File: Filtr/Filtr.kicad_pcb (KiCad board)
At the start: 2 copper layers, 80 x 50 mm, 41 parts, among them J1 Jack-DC, J2 Conn_01x04_Pin, SW3 RotaryEncoder_Switch, U1 TPS562200, U2 STM32G030K6Tx

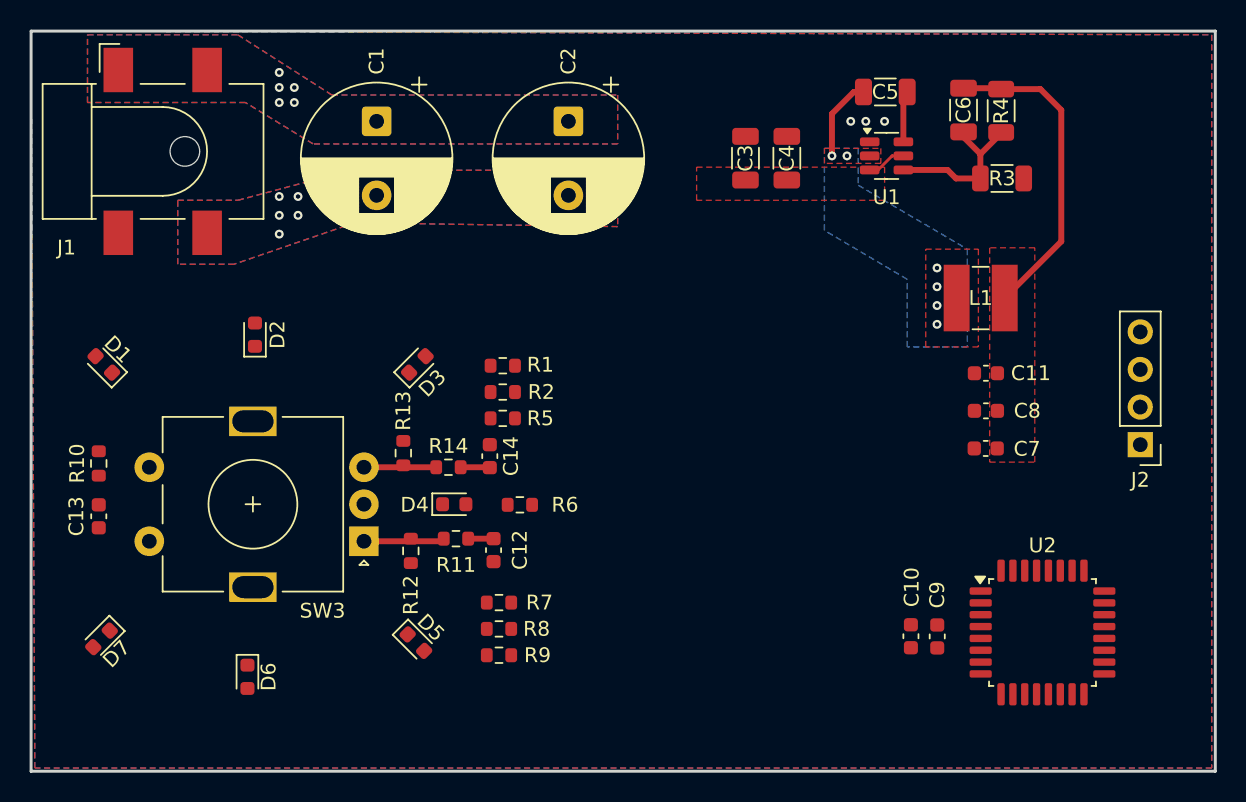
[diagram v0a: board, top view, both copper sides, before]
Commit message: Vymazani CubeIDE
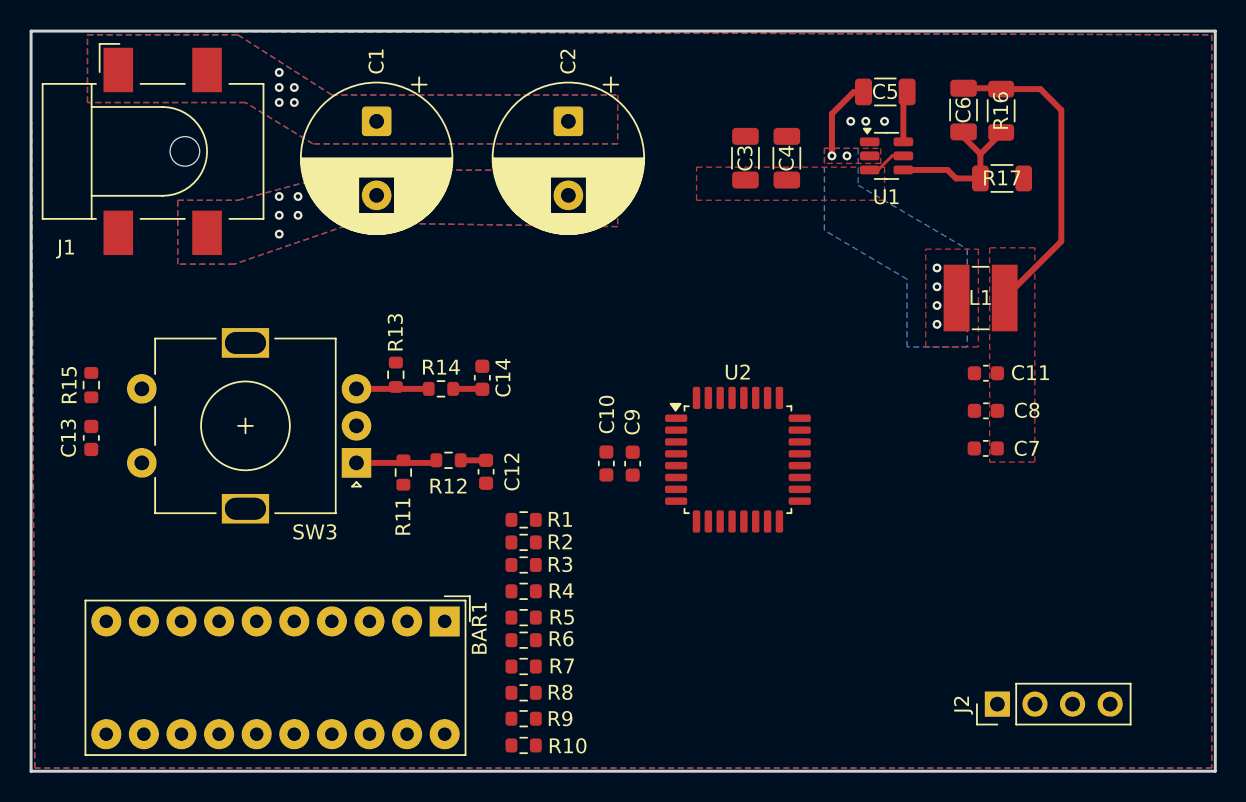
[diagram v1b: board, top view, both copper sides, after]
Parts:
- removed D1, D2, D3, D4, D5, D6, D7: LED, LED_SMD:LED_0603_1608Metric
- added BAR1: HDSP-4830, Display:HDSP-4830, F.Cu at (111.8, 61.5)
- added R10: R, Resistor_SMD:R_0603_1608Metric, F.Cu at (117.1, 69.8)
- added R8: R, Resistor_SMD:R_0603_1608Metric, F.Cu at (117.1, 66.3)
- added R9: R, Resistor_SMD:R_0603_1608Metric, F.Cu at (117.1, 68.0)
- moved C10 23.7 mm to (122.7, 50.8)
- moved C9 23.7 mm to (124.5, 50.8)
- moved U2 23.7 mm to (131.6, 50.5)
- moved J2 20.0 mm to (149.1, 67.1), turned to 90 degrees
- moved R7 18.6 mm to (117.1, 64.5)
- moved R6 18.6 mm to (117.1, 62.7)
- moved R1 7.00 mm to (117.1, 54.6)
- moved R12 5.32 mm to (112.0, 50.6)
- moved C12 5.32 mm to (114.6, 51.4)
- moved R14 5.32 mm to (111.5, 45.8)
- moved SW3 5.32 mm to (105.8, 50.8)
- moved C14 5.32 mm to (114.3, 45.0)
- moved R11 5.32 mm to (109.0, 51.4)
- moved C13 5.32 mm to (87.9, 49.1)
- moved R13 5.32 mm to (108.5, 44.8)
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- renumbered R5 to R1, R12 to R11, R11 to R12, R10 to R15, R4 to R16, R3 to R17, R6 to R2, R7 to R3, R8 to R4, R9 to R5, R1 to R6, R2 to R7
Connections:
- J2 pad 3: GND -> V+
- J2 pad 4: V+ -> GND
- R3 pad 2: Net-(D5-A) -> unconnected-(R3-Pad2)

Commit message: CubeIDE a Kicad
CubeIDE -nastaveni pinu
Kicad - pridani shift registru
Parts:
- added C15: 0.1u, Capacitor_SMD:C_0603_1608Metric, F.Cu at (127.3, 58.7)
- added U3: 74HC595, Package_SO:SO-16_5.3x10.2mm_P1.27mm, F.Cu at (123.1, 64.9)
- C10, C13, C9, R1, R10, R15, R2, R3, R4, R5, R6, R7, R8, R9: moved to B.Cu
- J1: value Jack-DC -> Barrel_Jack_Switch
- moved R1 29.6 mm to (88.9, 63.5), turned to 90 degrees
- moved R2 26.7 mm to (91.4, 63.5), turned to 90 degrees
- moved R3 23.8 mm to (94.0, 63.5), turned to 90 degrees
- moved R4 21.0 mm to (96.5, 63.6), turned to 90 degrees
- moved R5 18.2 mm to (99.1, 63.6), turned to 90 degrees
- moved J2 16.8 mm to (132.3, 68.3)
- moved R6 15.5 mm to (101.6, 63.5), turned to 90 degrees
- moved R7 13.0 mm to (104.1, 63.5), turned to 90 degrees
- moved R8 10.8 mm to (106.7, 63.5), turned to 90 degrees
- moved R9 9.09 mm to (109.2, 63.5), turned to 90 degrees
- moved R10 8.29 mm to (111.8, 63.5), turned to 90 degrees
- moved C13 6.16 mm to (94.0, 50.0)
- moved R15 6.16 mm to (94.0, 46.4)
- moved C9 5.85 mm to (119.6, 47.5)
- moved U2 4.72 mm to (128.1, 47.3)
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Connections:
- BAR1 pad 8: unconnected-(BAR1H-A-Pad8) -> Net-(BAR1H-A)
- J1 pad 3: (no net) -> GND
- R3 pad 2: unconnected-(R3-Pad2) -> Net-(BAR1H-A)
- U2 pad 12: unconnected-(U2-PA5-Pad12) -> BTN1
- U2 pad 15: BTN1 -> unconnected-(U2-PB0-Pad15)
- U2 pad 7: unconnected-(U2-PA0-Pad7) -> SER
- U2 pad 8: unconnected-(U2-PA1-Pad8) -> SRCLK
- U2 pad 9: unconnected-(U2-PA2-Pad9) -> RCLK
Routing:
- added copper zone on B.Cu, net (none)
- added copper zone on F.Cu, net (none)

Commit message: Novy Design desky
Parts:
- removed BAR1: HDSP-4830, Display:HDSP-4830
- removed C15: 0.1u, Capacitor_SMD:C_0603_1608Metric
- removed C2: C, Capacitor_THT:CP_Radial_D10.0mm_P5.00mm
- removed C6: C, Capacitor_SMD:C_1206_3216Metric
- removed R10, R7, R8, R9: R, Resistor_SMD:R_0603_1608Metric
- removed U3: 74HC595, Package_SO:SO-16_5.3x10.2mm_P1.27mm
- added H1: MountingHole_Pad, MountingHole:MountingHole_3.2mm_M3_DIN965_Pad, F.Cu at (169.9, 91.7)
- added H2: MountingHole_Pad, MountingHole:MountingHole_3.2mm_M3_DIN965_Pad, F.Cu at (169.9, 116.7)
- added H3: MountingHole_Pad, MountingHole:MountingHole_3.2mm_M3_DIN965_Pad, F.Cu at (254.9, 91.7)
- added H4: MountingHole_Pad, MountingHole:MountingHole_3.2mm_M3_DIN965_Pad, F.Cu at (254.9, 116.7)
- added J2: Conn_02x05_Odd_Even, Connector_PinHeader_2.54mm:PinHeader_2x05_P2.54mm_Vertical, F.Cu at (239.0, 93.2)
- added ProgConn1: Conn_01x04_Pin, Connector_PinHeader_2.54mm:PinHeader_1x04_P2.54mm_Vertical, F.Cu at (256.0, 97.0)
- C10, C9: moved to F.Cu
- C12, C14, C5, R11, R12, R13, R14: moved to B.Cu
- R6: footprint Resistor_SMD:R_0603_1608Metric -> Resistor_SMD:R_1206_3216Metric; moved to F.Cu
- moved R1 153.8 mm to (238.8, 98.0)
- moved R6 152.4 mm to (245.4, 114.0), turned to 0 degrees
- moved R2 149.6 mm to (237.0, 98.0)
- moved R3 145.4 mm to (235.2, 98.0)
- moved R4 141.2 mm to (233.4, 98.0)
- moved R5 137.0 mm to (231.6, 98.0)
- moved C12 131.0 mm to (228.9, 115.4)
- moved C14 131.0 mm to (228.6, 109.0)
- moved R11 131.0 mm to (223.3, 115.4)
- moved R12 131.0 mm to (226.3, 114.6)
- moved R13 131.0 mm to (222.8, 108.8)
- moved R14 131.0 mm to (225.8, 109.8)
- moved C9 130.7 mm to (238.3, 102.4)
- moved C13 130.5 mm to (207.5, 114.2)
- moved R15 130.5 mm to (207.5, 110.7)
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- renumbered J2 to Fan1
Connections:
- R6 pad 1: LED6 -> +3V3
- R6 pad 2: Net-(BAR1E-A) -> TACHO
- U2 pad 11: PWM -> unconnected-(U2-PA4-Pad11)
- U2 pad 16: unconnected-(U2-PB1-Pad16) -> PWM
- U2 pad 24: unconnected-(U2-PA13-Pad24) -> SWDIO
- U2 pad 25: unconnected-(U2-PA14-Pad25) -> SWCLK
- U2 pad 27: unconnected-(U2-PB3-Pad27) -> LED1
- U2 pad 28: unconnected-(U2-PB4-Pad28) -> LED2
- U2 pad 29: unconnected-(U2-PB5-Pad29) -> LED3
- U2 pad 30: unconnected-(U2-PB6-Pad30) -> LED4
- U2 pad 31: unconnected-(U2-PB7-Pad31) -> LED5
- U2 pad 7: SER -> unconnected-(U2-PA0-Pad7)
- U2 pad 8: SRCLK -> unconnected-(U2-PA1-Pad8)
- U2 pad 9: RCLK -> unconnected-(U2-PA2-Pad9)
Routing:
- net +3V3: track 21.5 -> 156.2 mm, vias 0 -> 3
- net BTN1: track 0.00 -> 46.4 mm, vias 0 -> 3
- net V+: track 2.67 -> 46.6 mm, vias 5 -> 2
- net ENC_A: track 1.72 -> 23.4 mm, vias 0 -> 1
- net ENC_B: track 1.98 -> 21.8 mm, vias 0 -> 1
- net TACHO: track 0.00 -> 17.5 mm
- net LED5: track 0.00 -> 16.3 mm, vias 0 -> 1
- net LED4: track 0.00 -> 15.1 mm, vias 0 -> 1
- net L1: track 5.58 -> 19.4 mm, vias 6 -> 7
- net PWM: track 0.00 -> 12.5 mm, vias 0 -> 2
- net LED3: track 0.00 -> 12.4 mm, vias 0 -> 1
- net Net-(J2-Pin_7): track 0.00 -> 12.2 mm
- net Net-(J2-Pin_9): track 0.00 -> 12.1 mm
- net Net-(J2-Pin_5): track 0.00 -> 11.3 mm
- net Net-(J2-Pin_3): track 0.00 -> 10.8 mm
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- removed copper zone on B.Cu, net (none)
- removed copper zone on F.Cu, net (none)
- removed copper zone on F.Cu, net +3V3
- removed copper zone on B.Cu, net L1
- removed copper zone on B.Cu, net V+
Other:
- board size 80 x 50 mm -> 92.2 x 31.8 mm
